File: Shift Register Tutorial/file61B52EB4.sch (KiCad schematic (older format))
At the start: 7 parts, among them Q201 2N3904, SW201 SW_Push

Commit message: Disconnect indicator LEDs
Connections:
- net DATA: no longer Q201.2 (B)
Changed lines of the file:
@@
 Text HLabel 2900 1600 2    50   Output ~ 0
 DATA
-Wire Wire Line
-	2000 1600 2400 1600
 Connection ~ 2000 1600
 Wire Wire Line
@@
 	1    0    0    -1
 $EndComp
-Wire Wire Line
-	2400 1600 2400 2400
-Wire Wire Line
-	2400 2400 3250 2400
-Connection ~ 2400 1600
-Wire Wire Line
-	2400 1600 2900 1600
 $Comp
 L power:GND #PWR0204
@@
 Wire Wire Line
 	3550 2000 3550 2200
+Wire Wire Line
+	2000 1600 2900 1600
 $EndSCHEMATC

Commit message: Rerouting board
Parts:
- removed D201: LED, LED_THT:LED_D5.0mm, symbol Device:LED
- removed Q201: 2N3904, Package_TO_SOT_THT:TO-92_Inline_Wide, symbol Transistor_BJT:2N3904
- removed R203: 2k2, Resistor_THT:R_Axial_DIN0207_L6.3mm_D2.5mm_P7.62mm_Horizontal, symbol Device:R
- C201: value 1u -> 10u
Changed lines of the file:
@@
 P 2000 1350
 F 0 "C201" H 2118 1396 50  0000 L CNN
-F 1 "1u" H 2118 1305 50  0000 L CNN
+F 1 "10u" H 2118 1305 50  0000 L CNN
 F 2 "Capacitor_THT:CP_Radial_D4.0mm_P2.00mm" H 2038 1200 50  0001 C CNN
 F 3 "~" H 2000 1350 50  0001 C CNN
@@
 Wire Wire Line
 	2000 1600 2000 1700
-$Comp
-L Transistor_BJT:2N3904 Q201
-U 1 1 61B59EAB
-P 3450 2400
-F 0 "Q201" H 3640 2446 50  0000 L CNN
-F 1 "2N3904" H 3640 2355 50  0000 L CNN
-F 2 "Package_TO_SOT_THT:TO-92_Inline_Wide" H 3650 2325 50  0001 L CIN
-F 3 "https://www.onsemi.com/pub/Collateral/2N3903-D.PDF" H 3450 2400 50  0001 L CNN
-	1    3450 2400
-	1    0    0    -1
-$EndComp
-$Comp
-L power:GND #PWR0204
-U 1 1 61B5B2C8
-P 3550 2950
-F 0 "#PWR0204" H 3550 2700 50  0001 C CNN
-F 1 "GND" H 3555 2777 50  0000 C CNN
-F 2 "" H 3550 2950 50  0001 C CNN
-F 3 "" H 3550 2950 50  0001 C CNN
-	1    3550 2950
-	1    0    0    -1
-$EndComp
-Wire Wire Line
-	3550 2600 3550 2950
-$Comp
-L Device:R R203
-U 1 1 61B5BEE6
-P 3550 1850
-F 0 "R203" H 3620 1896 50  0000 L CNN
-F 1 "2k2" H 3620 1805 50  0000 L CNN
-F 2 "Resistor_THT:R_Axial_DIN0207_L6.3mm_D2.5mm_P7.62mm_Horizontal" V 3480 1850 50  0001 C CNN
-F 3 "~" H 3550 1850 50  0001 C CNN
-	1    3550 1850
-	1    0    0    -1
-$EndComp
-$Comp
-L Device:LED D201
-U 1 1 61B5C33C
-P 3550 1350
-F 0 "D201" V 3589 1232 50  0000 R CNN
-F 1 "LED" V 3498 1232 50  0000 R CNN
-F 2 "LED_THT:LED_D5.0mm" H 3550 1350 50  0001 C CNN
-F 3 "~" H 3550 1350 50  0001 C CNN
-	1    3550 1350
-	0    -1   -1   0
-$EndComp
-$Comp
-L power:+5V #PWR0203
-U 1 1 61B5CCD1
-P 3550 950
-F 0 "#PWR0203" H 3550 800 50  0001 C CNN
-F 1 "+5V" H 3565 1123 50  0000 C CNN
-F 2 "" H 3550 950 50  0001 C CNN
-F 3 "" H 3550 950 50  0001 C CNN
-	1    3550 950
-	1    0    0    -1
-$EndComp
-Wire Wire Line
-	3550 950  3550 1200
-Wire Wire Line
-	3550 1500 3550 1700
-Wire Wire Line
-	3550 2000 3550 2200
 Wire Wire Line
 	2000 1600 2900 1600

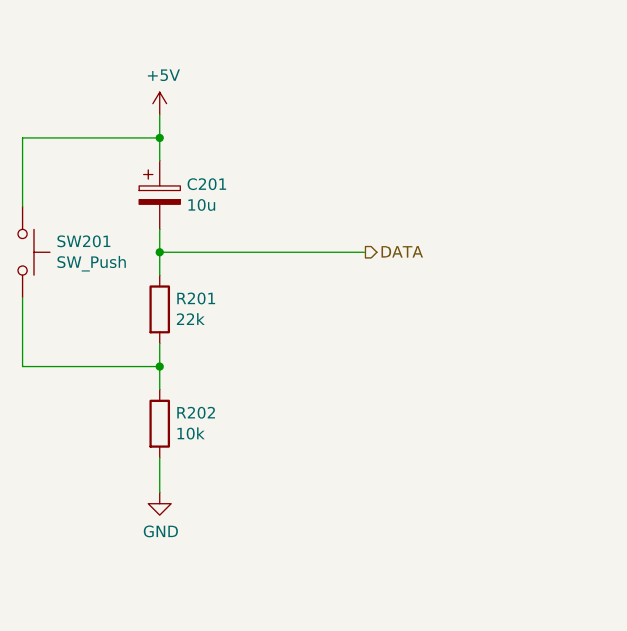
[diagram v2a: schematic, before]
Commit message: Another attempt at the Shift Registers (#12)
It appears that clock pins are very finicky about debouncing. Switch to using a 555 monostable for this purpose, and remove debounce from the other pins. The 'data' pin only matters on the clock edge, and the 'reset' pin is idempotent.
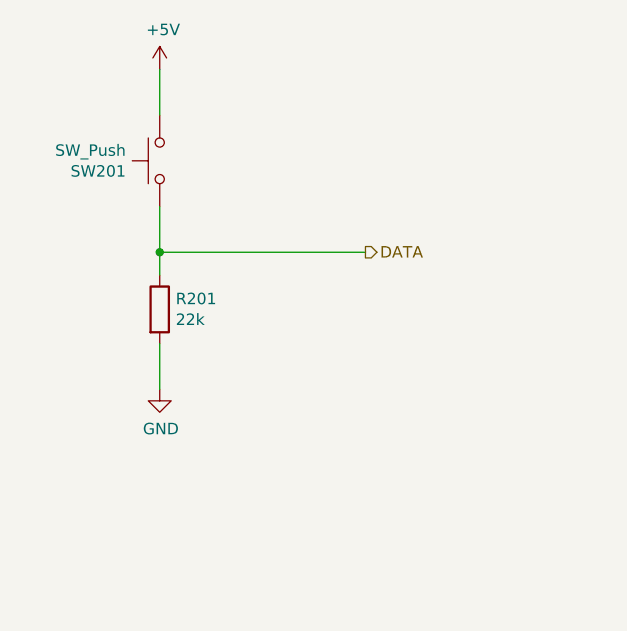
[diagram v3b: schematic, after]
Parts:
- removed C201: 10u, Capacitor_THT:CP_Radial_D4.0mm_P2.00mm, symbol Device:CP
- removed R202: 10k, Resistor_THT:R_Axial_DIN0207_L6.3mm_D2.5mm_P7.62mm_Horizontal, symbol Device:R
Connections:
- net +5V: now also SW201.2; no longer SW201.1
- net DATA: now also SW201.1
- net GND: now also R201.2
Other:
- moved on the sheet: SW201
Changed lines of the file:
@@
 $EndDescr
-$Comp
-L Device:R R202
-U 1 1 61B530DF
-P 2000 2350
-F 0 "R202" H 2070 2396 50  0000 L CNN
-F 1 "10k" H 2070 2305 50  0000 L CNN
-F 2 "Resistor_THT:R_Axial_DIN0207_L6.3mm_D2.5mm_P7.62mm_Horizontal" V 1930 2350 50  0001 C CNN
-F 3 "~" H 2000 2350 50  0001 C CNN
-	1    2000 2350
-	1    0    0    -1
-$EndComp
 $Comp
 L Device:R R201
@@
 $EndComp
 $Comp
-L Device:CP C201
-U 1 1 61B53C44
-P 2000 1350
-F 0 "C201" H 2118 1396 50  0000 L CNN
-F 1 "10u" H 2118 1305 50  0000 L CNN
-F 2 "Capacitor_THT:CP_Radial_D4.0mm_P2.00mm" H 2038 1200 50  0001 C CNN
-F 3 "~" H 2000 1350 50  0001 C CNN
-	1    2000 1350
-	1    0    0    -1
-$EndComp
-$Comp
 L power:+5V #PWR0201
 U 1 1 61B54320
-P 2000 1000
-F 0 "#PWR0201" H 2000 850 50  0001 C CNN
-F 1 "+5V" H 2015 1173 50  0000 C CNN
-F 2 "" H 2000 1000 50  0001 C CNN
-F 3 "" H 2000 1000 50  0001 C CNN
-	1    2000 1000
+P 2000 800
+F 0 "#PWR0201" H 2000 650 50  0001 C CNN
+F 1 "+5V" H 2015 973 50  0000 C CNN
+F 2 "" H 2000 800 50  0001 C CNN
+F 3 "" H 2000 800 50  0001 C CNN
+	1    2000 800
 	1    0    0    -1
 $EndComp
@@
 L power:GND #PWR0202
 U 1 1 61B546EC
-P 2000 2650
-F 0 "#PWR0202" H 2000 2400 50  0001 C CNN
-F 1 "GND" H 2005 2477 50  0000 C CNN
-F 2 "" H 2000 2650 50  0001 C CNN
-F 3 "" H 2000 2650 50  0001 C CNN
-	1    2000 2650
+P 2000 2200
+F 0 "#PWR0202" H 2000 1950 50  0001 C CNN
+F 1 "GND" H 2005 2027 50  0000 C CNN
+F 2 "" H 2000 2200 50  0001 C CNN
+F 3 "" H 2000 2200 50  0001 C CNN
+	1    2000 2200
 	1    0    0    -1
 $EndComp
-Wire Wire Line
-	2000 1000 2000 1100
-Wire Wire Line
-	2000 1500 2000 1600
-Wire Wire Line
-	2000 2000 2000 2100
-Wire Wire Line
-	2000 2500 2000 2650
 $Comp
 L Switch:SW_Push SW201
 U 1 1 61B57C55
-P 1400 1600
-F 0 "SW201" V 1354 1748 50  0000 L CNN
-F 1 "SW_Push" V 1445 1748 50  0000 L CNN
-F 2 "Button_Switch_THT:SW_PUSH_6mm_H4.3mm" H 1400 1800 50  0001 C CNN
-F 3 "~" H 1400 1800 50  0001 C CNN
-	1    1400 1600
-	0    1    1    0
+P 2000 1200
+F 0 "SW201" V 1954 1348 50  0000 L CNN
+F 1 "SW_Push" V 2045 1348 50  0000 L CNN
+F 2 "Button_Switch_THT:SW_PUSH_6mm_H4.3mm" H 2000 1400 50  0001 C CNN
+F 3 "~" H 2000 1400 50  0001 C CNN
+	1    2000 1200
+	0    -1   -1   0
 $EndComp
-Wire Wire Line
-	1400 1800 1400 2100
-Wire Wire Line
-	1400 2100 2000 2100
-Connection ~ 2000 2100
-Wire Wire Line
-	2000 2100 2000 2200
-Wire Wire Line
-	1400 1400 1400 1100
-Wire Wire Line
-	1400 1100 2000 1100
-Connection ~ 2000 1100
-Wire Wire Line
-	2000 1100 2000 1200
 Text HLabel 2900 1600 2    50   Output ~ 0
 DATA
@@
 Wire Wire Line
 	2000 1600 2900 1600
+Wire Wire Line
+	2000 2000 2000 2200
+Wire Wire Line
+	2000 1000 2000 800
+Wire Wire Line
+	2000 1400 2000 1600
 $EndSCHEMATC
